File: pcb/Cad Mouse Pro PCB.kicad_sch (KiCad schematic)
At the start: 18 parts, among them J1 Conn_01x12_Pin, J2 Conn_01x12_Pin

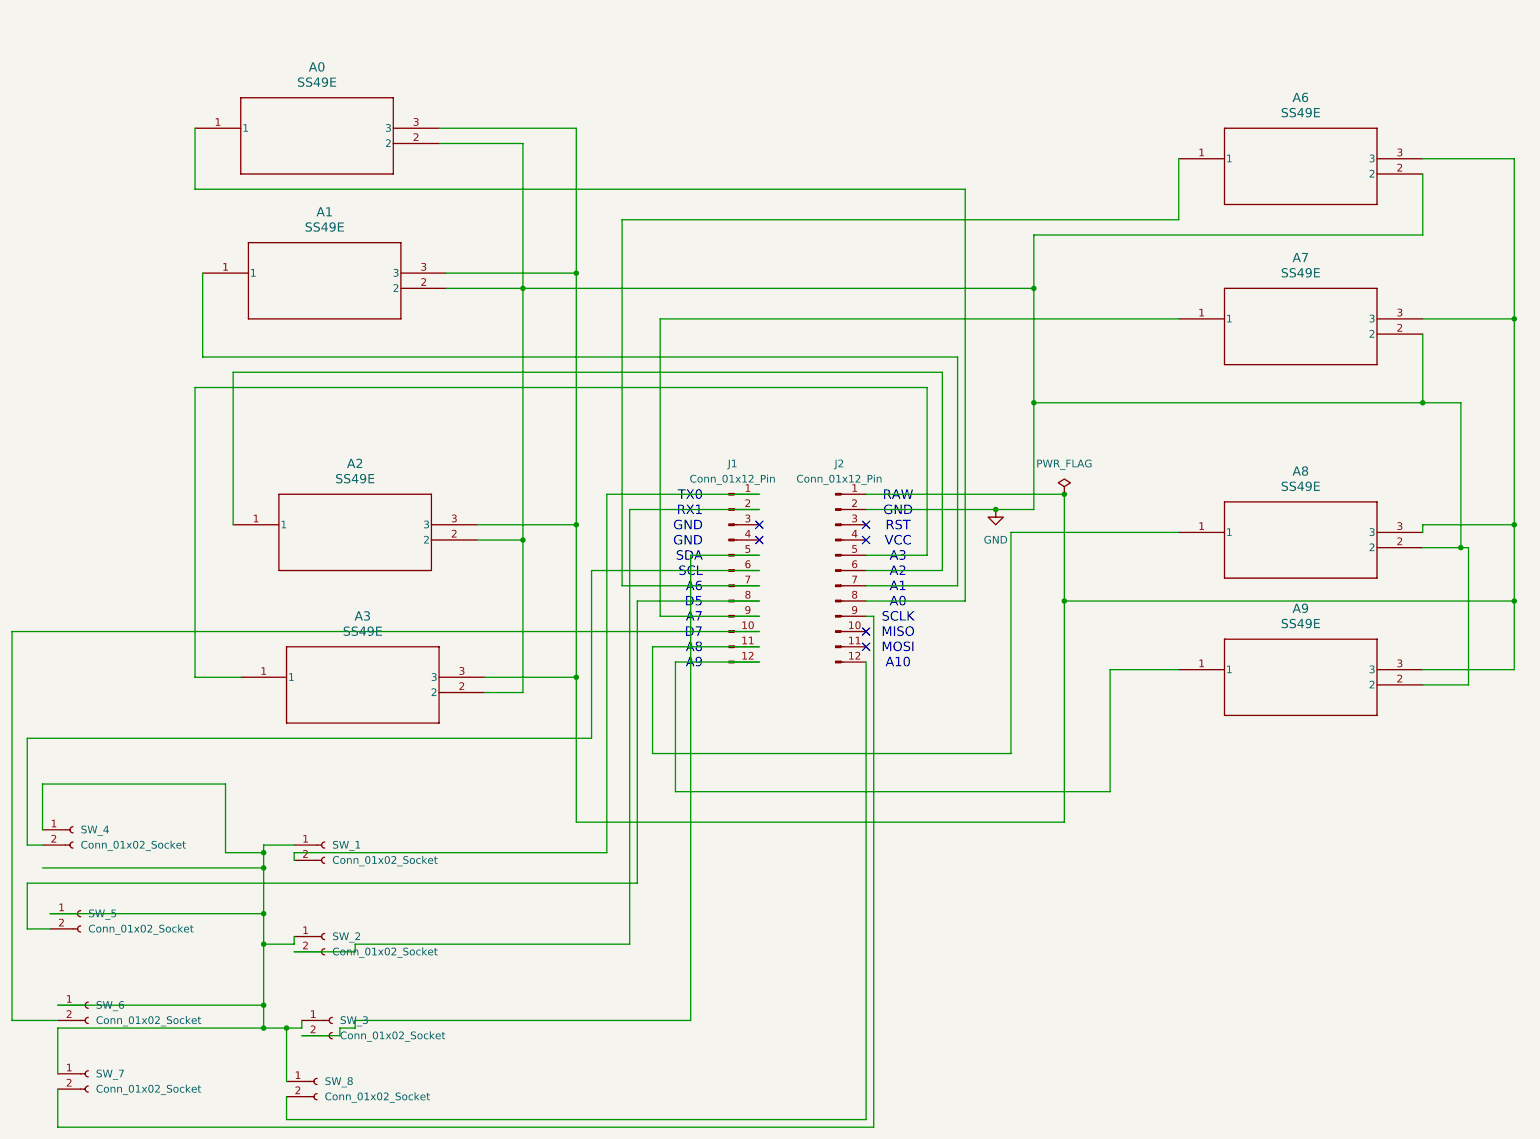
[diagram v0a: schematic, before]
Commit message: Added pro micro submodul and connectors for debugging
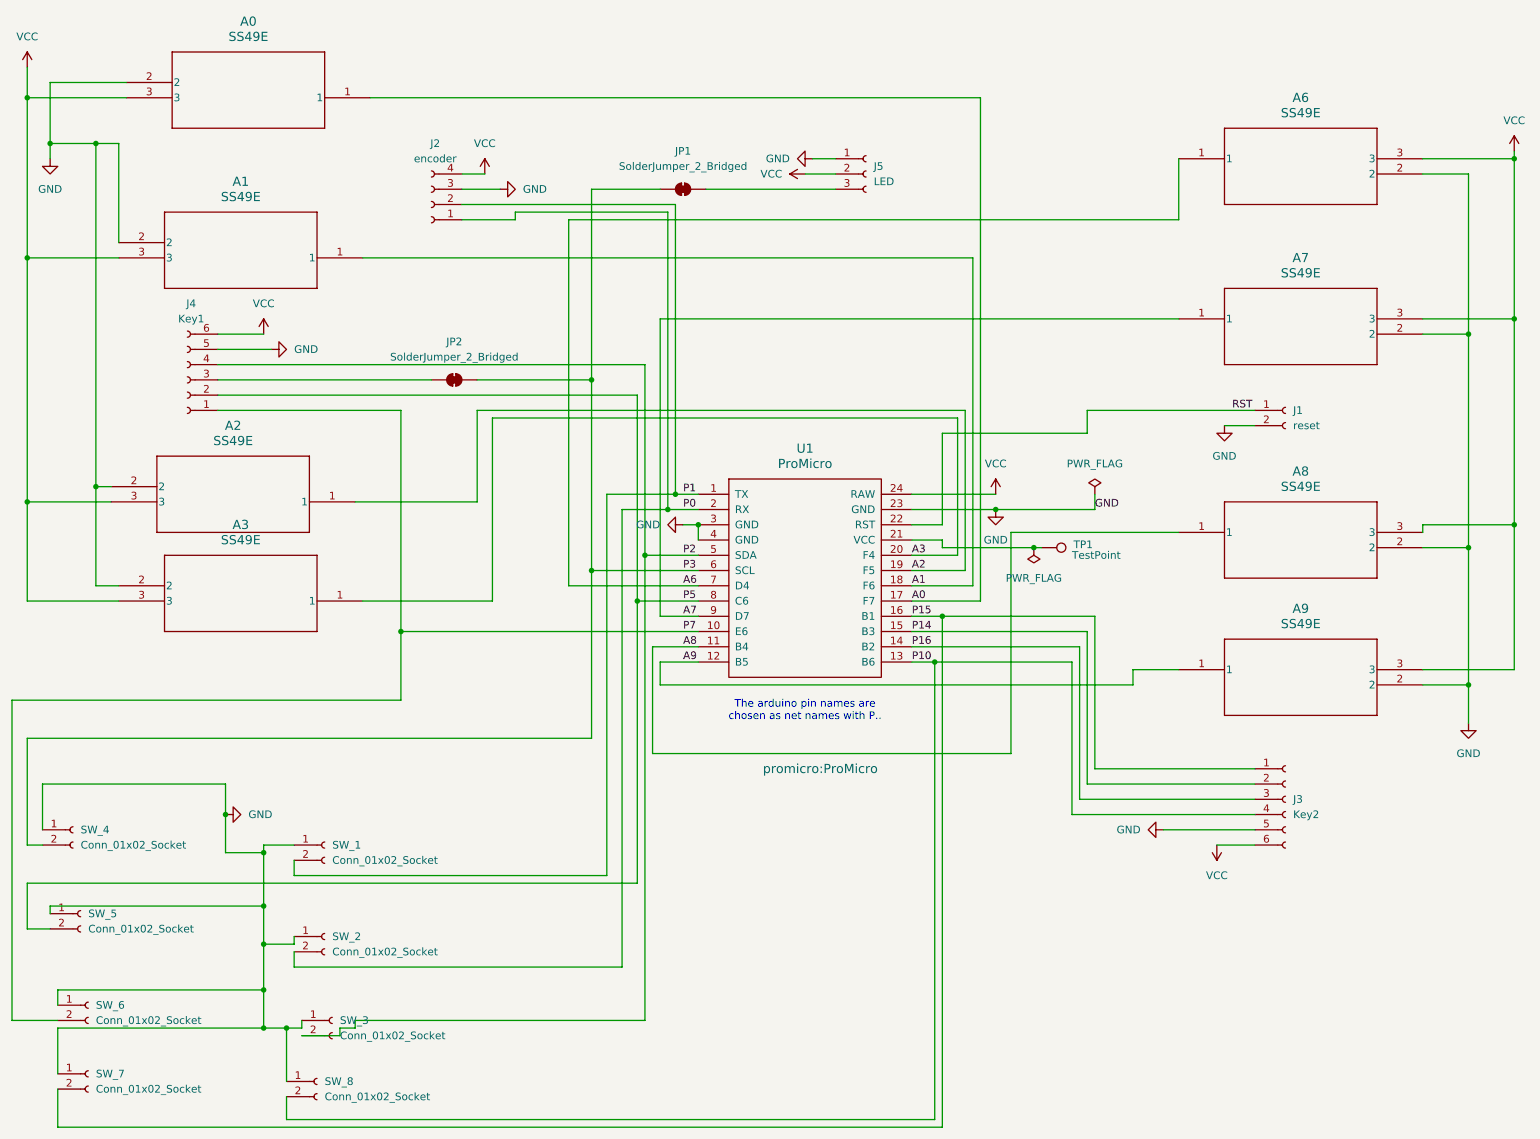
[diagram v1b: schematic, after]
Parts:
- removed J1, J2: Conn_01x12_Pin, Connector_PinHeader_2.54mm:PinHeader_1x12_P2.54mm_Vertical, symbol Connector:Conn_01x12_Pin
- added J1: reset, Connector_JST:JST_XH_S2B-XH-A-1_1x02_P2.50mm_Horizontal, symbol Connector:Conn_01x02_Socket
- added J2: encoder, Connector_JST:JST_XH_S4B-XH-A-1_1x04_P2.50mm_Horizontal, symbol Connector:Conn_01x04_Socket
- added J3: Key2, Connector_JST:JST_XH_S6B-XH-A-1_1x06_P2.50mm_Horizontal, symbol Connector:Conn_01x06_Socket
- added J4: Key1, Connector_JST:JST_XH_S6B-XH-A-1_1x06_P2.50mm_Horizontal, symbol Connector:Conn_01x06_Socket
- added J5: LED, Connector_JST:JST_XH_S3B-XH-A-1_1x03_P2.50mm_Horizontal, symbol Connector:Conn_01x03_Socket
- added JP1, JP2: SolderJumper_2_Bridged, Jumper:SolderJumper-2_P1.3mm_Bridged2Bar_RoundedPad1.0x1.5mm, symbol Jumper:SolderJumper_2_Bridged
- added TP1: TestPoint, TestPoint:TestPoint_Plated_Hole_D2.0mm, symbol Connector:TestPoint
- added U1: ProMicro, promicro:ProMicro, symbol ProMicroKiCad:ProMicro
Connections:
- net GND: now also SW_1.1 (Pin_1), SW_2.1 (Pin_1), SW_3.1 (Pin_1), SW_4.1 (Pin_1), SW_5.1 (Pin_1), SW_6.1 (Pin_1), SW_7.1 (Pin_1), SW_8.1 (Pin_1), J1.2 (Pin_2), J2.3 (Pin_3), J3.5 (Pin_5), J4.5 (Pin_5), J5.1 (Pin_1), U1.23 (GND), U1.3 (GND), U1.4 (GND)
- net A0: now reaches A0.1
- net A0: now also U1.17 (F7)
- net VCC: now reaches A0.3, A1.3, A2.3, A3.3, A6.3, A7.3, A8.3, A9.3
- net VCC: now also J2.4 (Pin_4), J3.6 (Pin_6), J4.6 (Pin_6), J5.2 (Pin_2), U1.24 (RAW)
- net A6: now reaches A6.1
- net A6: now also U1.7 (D4)
- net P10: now reaches SW_8.2 (Pin_2)
- net P10: now also J3.4 (Pin_4), U1.13 (B6)
- net P15: now reaches SW_7.2 (Pin_2)
- net P15: now also J3.1 (Pin_1), U1.16 (B1)
- net A8: now reaches A8.1
- net A8: now also U1.11 (B4)
- net A3: now reaches A3.1
- net A3: now also U1.20 (F4)
- net P1: now reaches SW_1.2 (Pin_2)
- net P1: now also J2.2 (Pin_2), U1.1 (TX)
- net P7: now reaches SW_6.2 (Pin_2)
- net P7: now also J4.1 (Pin_1), U1.10 (E6)
- net A9: now reaches A9.1
- net A9: now also U1.12 (B5)
- net P0: now reaches SW_2.2 (Pin_2)
- net P0: now also J2.1 (Pin_1), U1.2 (RX)
- net P2: now reaches SW_3.2 (Pin_2)
- net P2: now also J4.4 (Pin_4), U1.5 (SDA)
- net P3: now reaches SW_4.2 (Pin_2)
- net P3: now also JP1.2 (B), JP2.1 (A), U1.6 (SCL)
- net P5: now reaches SW_5.2 (Pin_2)
- net P5: now also J4.2 (Pin_2), U1.8 (C6)
- net A7: now reaches A7.1
- net A7: now also U1.9 (D7)
- net A2: now reaches A2.1
- net A2: now also U1.19 (F5)
- net A1: now reaches A1.1
- net A1: now also U1.18 (F6)
- new net: TP1.1, U1.21 (VCC)
- new net: J5.3 (Pin_3), JP1.1 (A)
- new net: J4.3 (Pin_3), JP2.2 (B)
- new net P14: J3.2 (Pin_2), U1.15 (B3)
- new net P16: J3.3 (Pin_3), U1.14 (B2)
- new net RST: J1.1 (Pin_1), U1.22 (RST)
- no-connect marks 6 -> 0
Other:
- note added: "The arduino pin names are chosen as net names with P.."
- note removed: "RAW GND RST VCC A3 A2 A1 A0 SCLK MISO MOSI A10"
- note removed: "TX0 RX1 GND GND SDA SCL A6 D5 A7 D7 A8 A9"
- company: (none) -> Andun_HH
- title: (none) -> Space Mouse - Hall Effect - Arduino Pro Micro
- moved on the sheet: A0, A1, A2, A3
